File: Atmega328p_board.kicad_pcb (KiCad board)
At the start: 2 copper layers, 48.2 x 30.3 mm, 30 parts, among them J1 Conn_01x04_Pin, J2 Conn_01x04_Pin, J3 Conn_01x09_Pin, J4 Conn_02x03_Odd_Even, U1 24LC1025, U2 24LC1025, U3 ATMEGA328P-AU, U4 DS1337S_, Y1 16MHz, Y2 32.768 KHz

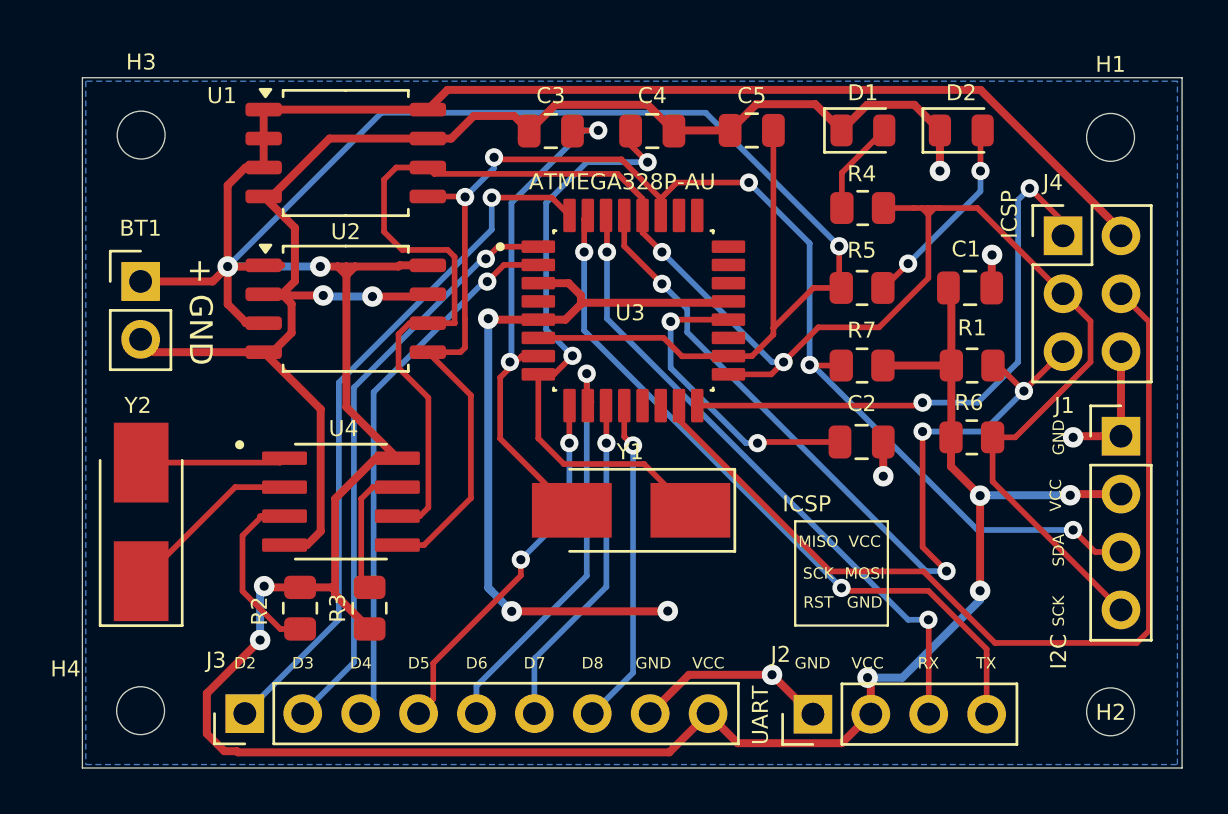
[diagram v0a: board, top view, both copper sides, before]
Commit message: gitignore updated
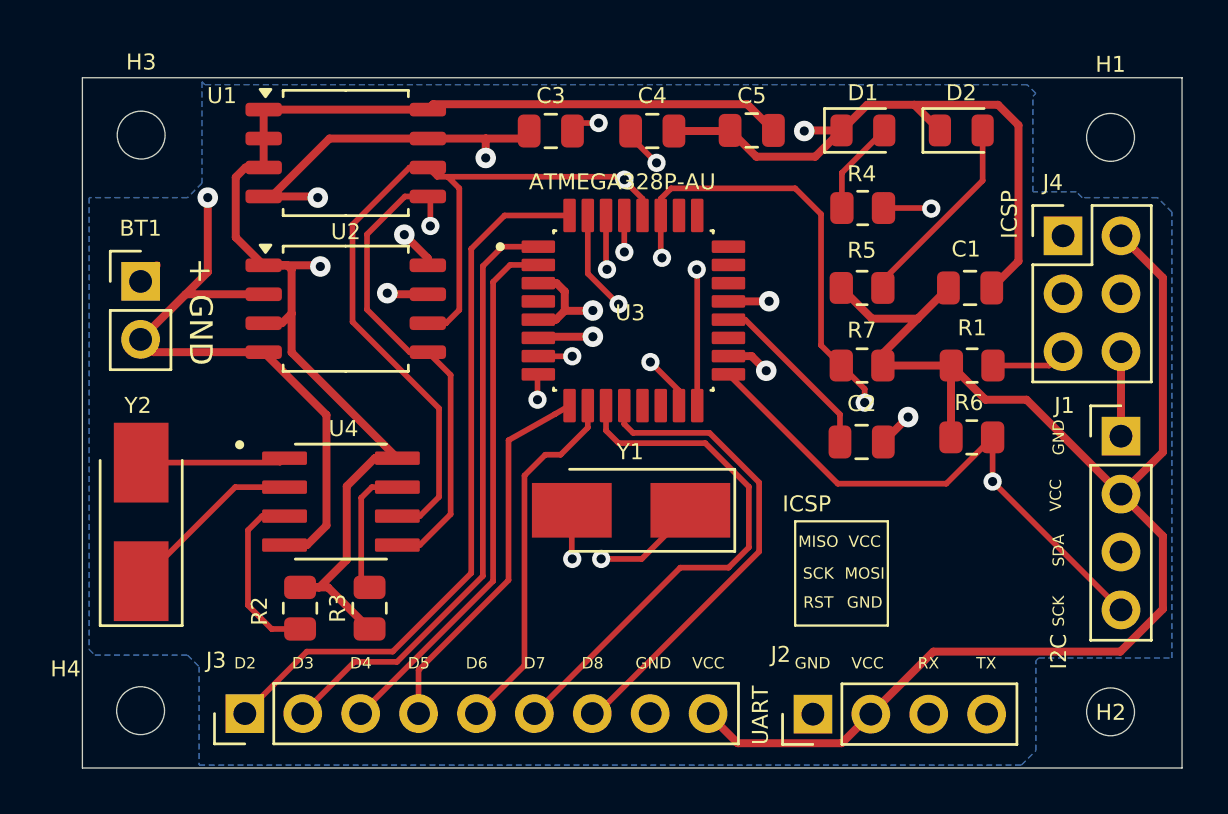
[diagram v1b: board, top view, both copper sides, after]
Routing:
- net /VCC: track 218.7 -> 154.2 mm, vias 9 -> 4
- net GND: track 120.5 -> 85.9 mm, vias 10 -> 8
- net /MOSI: track 40.8 -> 24.3 mm, vias 0 -> 1
- net /RESET: track 38.8 -> 26.0 mm, vias 4 -> 1
- net /SCK: track 86.5 -> 97.3 mm, vias 2 -> 3
- net /D7: track 14.8 -> 23.5 mm, vias 1 -> 0
- net /D8: track 14.4 -> 21.1 mm, vias 1 -> 0
- net Net-(U3-AREF): track 13.4 -> 7.82 mm, vias 2 -> 0
- net Net-(U3-PB7): track 26.7 -> 30.4 mm, vias 2 -> 3
- net /MISO: track 25.4 -> 22.7 mm, vias 2 -> 1
- net /D6: track 18.6 -> 15.9 mm, vias 1 -> 0
- net Net-(U3-PB6): track 22.5 -> 24.5 mm, vias 2 -> 3
- net /SDA: track 64.5 -> 65.9 mm, vias 5 -> 3
- net /TX: track 31.4 -> 32.7 mm, vias 2 -> 1
- net Net-(U4-~{INTA}): track 8.93 -> 7.87 mm
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- added copper zone on In2.Cu, net /VCC
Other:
- copper layers 2 -> 4
